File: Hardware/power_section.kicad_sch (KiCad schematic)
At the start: 38 parts, among them IC2 TPS54202HDDCR, U4 TLV743P, U6 TLV743P, U7 TLV743P

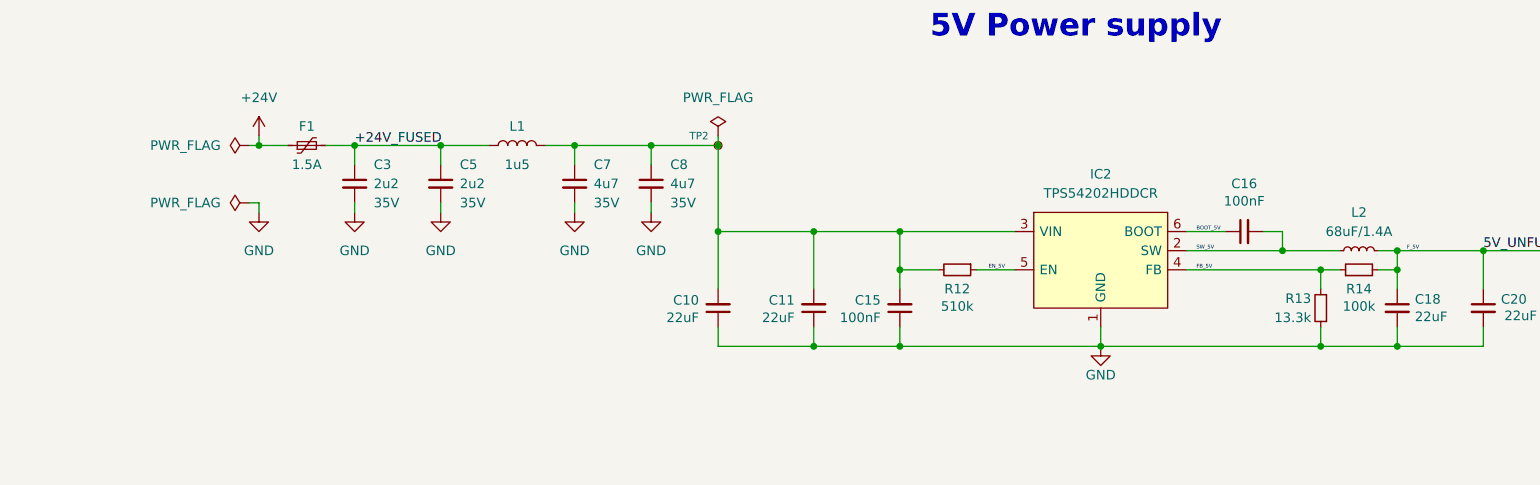
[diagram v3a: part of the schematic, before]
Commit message: Changes Vcc op-amps in brakes pressure (3V3 to 5V) and mcp6002 footprint (to MSOP8)
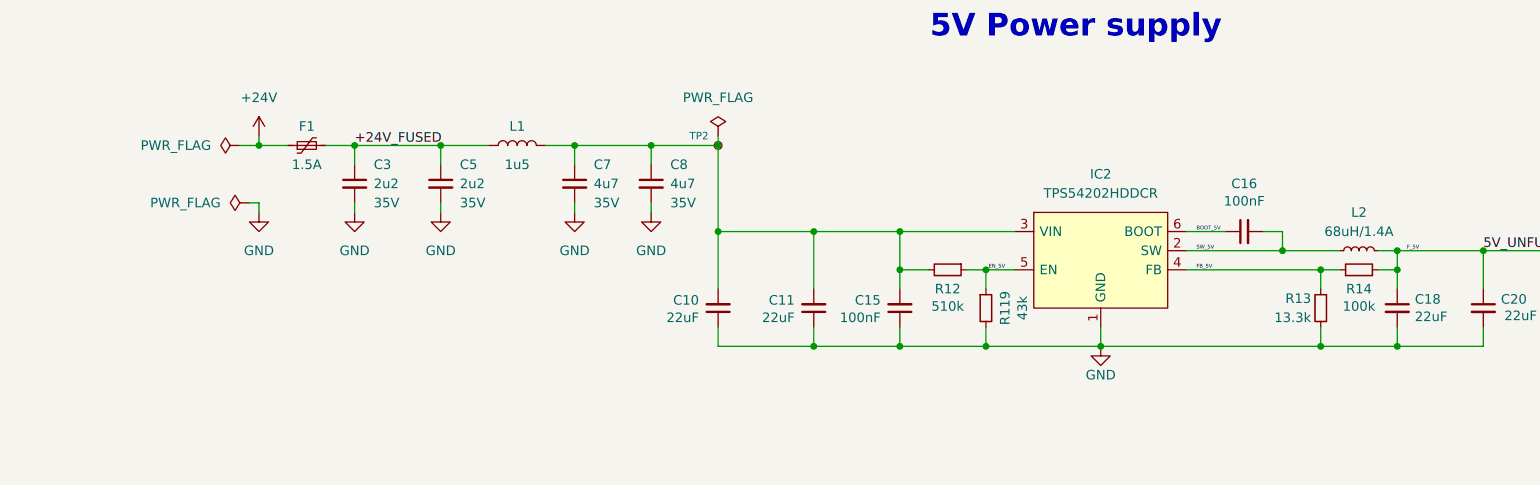
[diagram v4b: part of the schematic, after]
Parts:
- added R119: 43k, Resistor_SMD:R_0603_1608Metric, symbol Device:R_Small
- L2: value 68uF/1.4A -> 68uH/1.4A
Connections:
- net EN_5V: now also R119.1
- net GND: now also R119.2
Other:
- moved on the sheet: R12

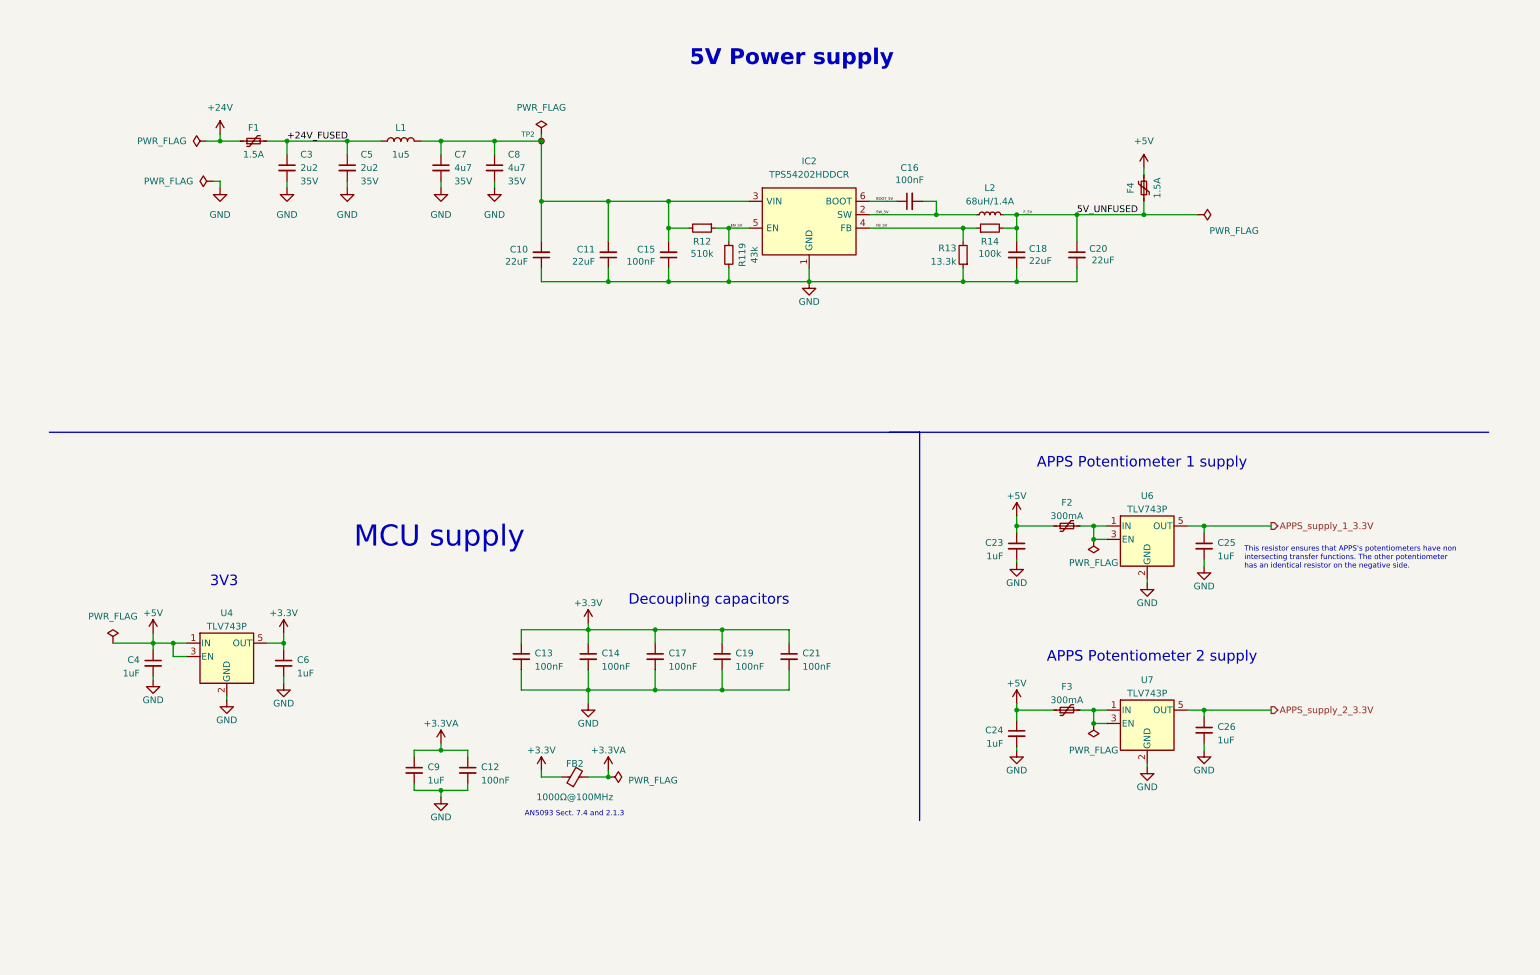
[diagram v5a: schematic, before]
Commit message: Created new hardware version 2.0
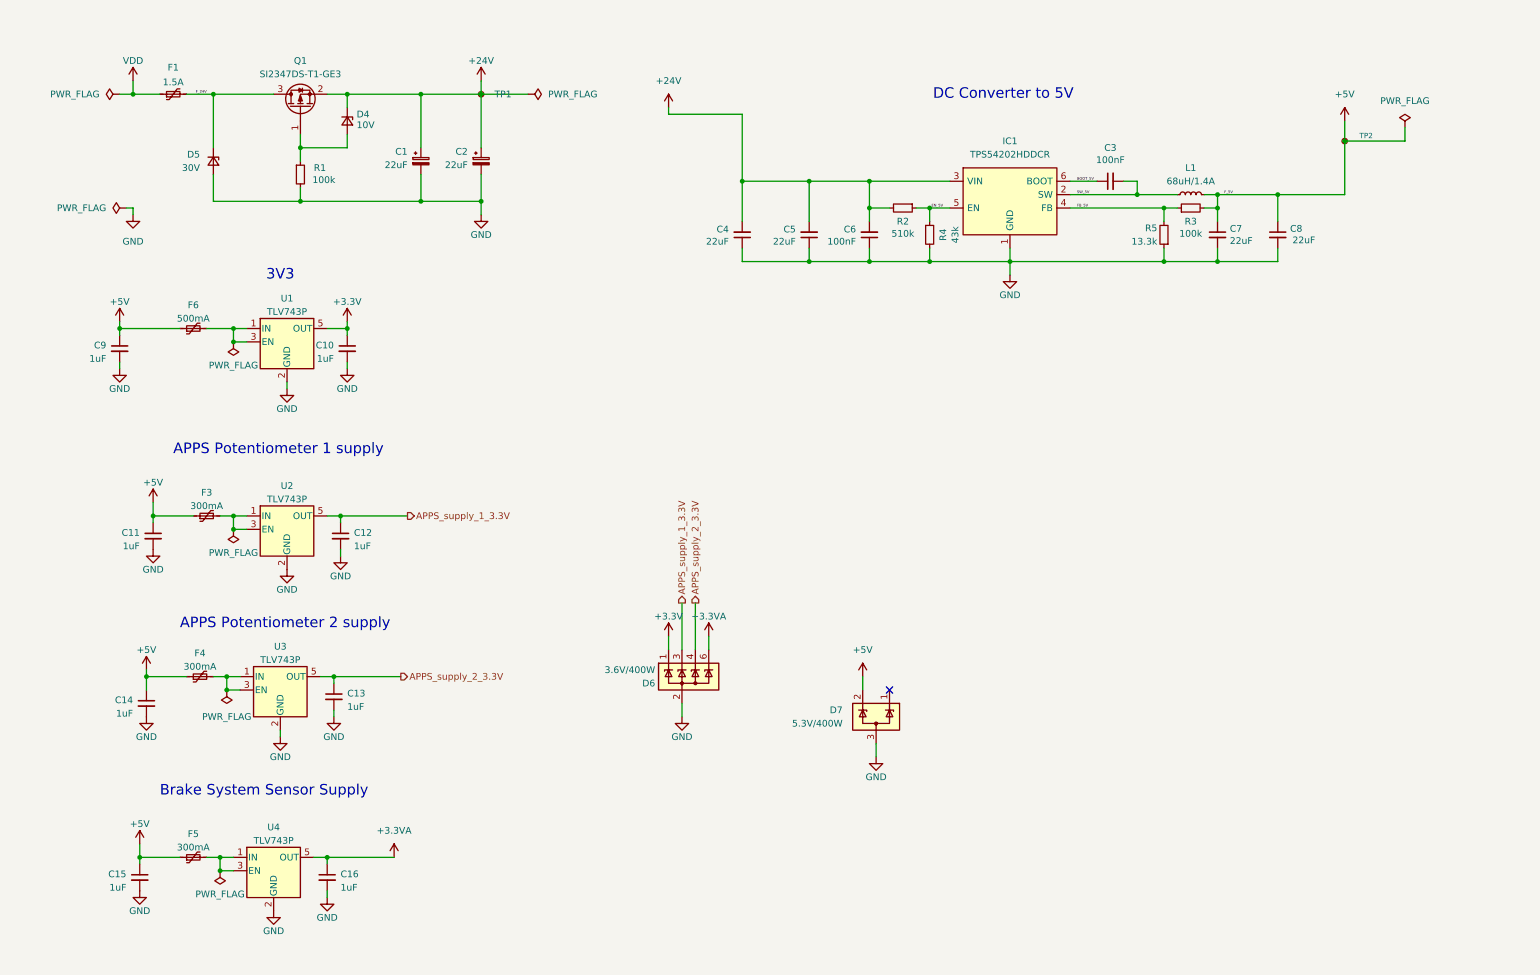
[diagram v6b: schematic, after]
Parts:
- removed C11, C18, C20: 22uF, Capacitor_SMD:C_0805_2012Metric, symbol Device:C_Small
- removed C12, C13, C14, C17, C19, C21: 100nF, Capacitor_SMD:C_0402_1005Metric_Pad0.74x0.62mm_HandSolder, symbol Device:C_Small
- removed F4: 1.5A, Fuse:Fuse_1812_4532Metric, symbol Device:Polyfuse_Small
- removed FB2: 1000Ω@100MHz, Inductor_SMD:L_0603_1608Metric, symbol Device:FerriteBead_Small
- removed L1: 1u5, Inductor_SMD:L_Abracon_ASPI-4030S, symbol Device:L
- removed R12: 510k, Resistor_SMD:R_0603_1608Metric, symbol Device:R_Small
- removed R13: 13.3k, Resistor_SMD:R_0603_1608Metric, symbol Device:R_Small
- removed R14: 100k, Resistor_SMD:R_0603_1608Metric, symbol Device:R_Small
- removed U6, U7: TLV743P, Package_TO_SOT_SMD:SOT-23-5_HandSoldering, symbol Regulator_Linear:TLV73330PDBV
- added C1, C2: 22uF, Capacitor_SMD:CP_Elec_4x5.8, symbol Device:C_Polarized_Small
- added D4: 10V, Diode_SMD:D_SOD-123, symbol Device:D_Zener_Small
- added D5: 30V, Diode_SMD:D_SOD-123, symbol Device:D_Zener_Small
- added D6: 3.6V/400W, Package_TO_SOT_SMD:SOT-23-6, symbol Power_Protection:ESDA5V3SC5
- added D7: 5.3V/400W, Package_TO_SOT_SMD:SOT-23-3, symbol Power_Protection:ESDA5V3L
- added F5: 300mA, Fuse:Fuse_0603_1608Metric_Pad1.05x0.95mm_HandSolder, symbol Device:Polyfuse_Small
- added F6: 500mA, Fuse:Fuse_0603_1608Metric_Pad1.05x0.95mm_HandSolder, symbol Device:Polyfuse_Small
- added Q1: SI2347DS-T1-GE3, Package_TO_SOT_SMD:SOT-23-3, symbol Transistor_FET:Q_PMOS_GSD
- added R1: 100k, Resistor_SMD:R_0603_1608Metric_Pad0.98x0.95mm_HandSolder, symbol Device:R_Small
- added R2: 510k, Resistor_SMD:R_0603_1608Metric, symbol Device:R_Small
- added R3: 100k, Resistor_SMD:R_0603_1608Metric, symbol Device:R_Small
- added R5: 13.3k, Resistor_SMD:R_0603_1608Metric, symbol Device:R_Small
- added TP1: TestPoint_Small, TestPoint:TestPoint_THTPad_D1.0mm_Drill0.5mm, symbol Connector:TestPoint_Small
- added U1, U2, U3: TLV743P, Package_TO_SOT_SMD:SOT-23-5_HandSoldering, symbol Regulator_Linear:TLV73330PDBV
- C10: value 22uF -> 1uF; footprint Capacitor_SMD:C_0805_2012Metric -> Capacitor_SMD:C_0603_1608Metric_Pad1.08x0.95mm_HandSolder; Manufacturer_Name MCASH21GCC7684MTCA1J -> (none); Manufacturer_Part_Number CL21A107MQYNNWE -> (none); Mouser Part Number 810-C2012X5R1V226MAC -> (none)
- C11: renamed from C23; footprint Capacitor_SMD:C_0402_1005Metric_Pad0.74x0.62mm_HandSolder -> Capacitor_SMD:C_0603_1608Metric_Pad1.08x0.95mm_HandSolder
- C12: renamed from C25; footprint Capacitor_SMD:C_0402_1005Metric_Pad0.74x0.62mm_HandSolder -> Capacitor_SMD:C_0603_1608Metric_Pad1.08x0.95mm_HandSolder
- C13: renamed from C26; footprint Capacitor_SMD:C_0402_1005Metric_Pad0.74x0.62mm_HandSolder -> Capacitor_SMD:C_0603_1608Metric_Pad1.08x0.95mm_HandSolder
- C14: renamed from C24; footprint Capacitor_SMD:C_0402_1005Metric_Pad0.74x0.62mm_HandSolder -> Capacitor_SMD:C_0603_1608Metric_Pad1.08x0.95mm_HandSolder
- C15, C16: value 100nF -> 1uF; footprint Capacitor_SMD:C_0603_1608Metric -> Capacitor_SMD:C_0603_1608Metric_Pad1.08x0.95mm_HandSolder; Manufacturer_Name -- -> (none); Manufacturer_Part_Number C0603C104J3RACTU -> (none); Mouser Part Number -- -> (none); Mouser Price/Stock https://www.mouser.pl/ProductDetail/KEMET/C0603C104J3RACTU?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 -> (none)
- C3: value 2u2 -> 100nF; footprint Capacitor_SMD:C_0805_2012Metric -> Capacitor_SMD:C_0603_1608Metric; Manufacturer_Name (none) -> --; Manufacturer_Part_Number (none) -> C0603C104J3RACTU; Mouser Part Number (none) -> --; Mouser Price/Stock (none) -> https://www.mouser.pl/ProductDetail/KEMET/C0603C104J3RACTU?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; Rated Voltage 35V -> (none)
- C4: value 1uF -> 22uF; footprint Capacitor_SMD:C_0402_1005Metric_Pad0.74x0.62mm_HandSolder -> Capacitor_SMD:C_0805_2012Metric; Manufacturer_Name (none) -> MCASH21GCC7684MTCA1J; Manufacturer_Part_Number (none) -> CL21A107MQYNNWE; Mouser Part Number (none) -> 810-C2012X5R1V226MAC
- C5: value 2u2 -> 22uF; Manufacturer_Name (none) -> MCASH21GCC7684MTCA1J; Manufacturer_Part_Number (none) -> CL21A107MQYNNWE; Mouser Part Number (none) -> 810-C2012X5R1V226MAC; Rated Voltage 35V -> (none)
- C6: value 1uF -> 100nF; footprint Capacitor_SMD:C_0402_1005Metric_Pad0.74x0.62mm_HandSolder -> Capacitor_SMD:C_0603_1608Metric; Manufacturer_Name (none) -> --; Manufacturer_Part_Number (none) -> C0603C104J3RACTU; Mouser Part Number (none) -> --; Mouser Price/Stock (none) -> https://www.mouser.pl/ProductDetail/KEMET/C0603C104J3RACTU?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
- C7, C8: value 4u7 -> 22uF; Manufacturer_Name (none) -> MCASH21GCC7684MTCA1J; Manufacturer_Part_Number (none) -> CL21A107MQYNNWE; Mouser Part Number (none) -> 810-C2012X5R1V226MAC; Rated Voltage 35V -> (none)
- C9: footprint Capacitor_SMD:C_0402_1005Metric_Pad0.74x0.62mm_HandSolder -> Capacitor_SMD:C_0603_1608Metric_Pad1.08x0.95mm_HandSolder
- renumbered F2 to F3, F3 to F4, IC2 to IC1, L2 to L1, R119 to R4
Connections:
- net 5V_UNFUSED is gone; now on net +5V: L1.2
- net +24V: now also C4.2, C5.2, C6.2, IC1.3 (VIN), C1.1, C2.1, D4.1 (K), Q1.2 (S), R2.2, TP1.1; no longer F1.1
- net +3.3V: now also C10.1, D6.1 (A), U1.5 (OUT); no longer C6.1, U4.5 (OUT)
- net +3.3VA: now also C16.1, U4.5 (OUT), D6.6 (A); no longer C9.1
- net +5V: now also C15.1, C7.1, C8.1, C9.1, TP2.1, D7.2 (K), F5.1, F6.1, R3.2; no longer C4.1, U4.1 (IN), U4.3 (EN)
- net APPS_supply_1_3.3V: now also D6.3 (A), U2.5 (OUT)
- net APPS_supply_2_3.3V: now also D6.4 (A), U3.5 (OUT)
- net BOOT_5V: now also C3.1; no longer C16.1
- net EN_5V: now also R2.1
- net FB_5V: now also R3.1, R5.2
- net GND: now also C10.2, C15.2, C16.2, C4.1, C5.1, C6.1, C1.2, C2.2, D5.2 (A), D6.2 (K), D6.5 (NC), D7.3 (A), R1.2, R5.1, U1.2 (GND), U2.2 (GND), U3.2 (GND); no longer C10.1, C15.1, C3.2, C4.2, C5.2, C6.2
- net SW_5V: now also C3.2; no longer C16.2
- net at F4.2: now also U3.1 (IN), U3.3 (EN)
- net at F3.2: now also U2.1 (IN), U2.3 (EN)
- removed net +24V_FUSED: C3.1, C5.1, F1.2
- new net: D4.2 (A), Q1.1 (G), R1.1
- new net: F5.2, U4.1 (IN), U4.3 (EN)
- new net: F6.2, U1.1 (IN), U1.3 (EN)
- new net F_24V: D5.1 (K), F1.2, Q1.3 (D)
- new net VDD: F1.1
- no-connect marks 0 -> 1
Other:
- note added: "Brake System Sensor Supply"
- note added: "DC Converter to 5V"
- note removed: "5V Power supply"
- note removed: "AN5093 Sect. 7.4 and 2.1.3"
- note removed: "Decoupling capacitors"
- note removed: "MCU supply"
- note removed: "This resistor ensures that APPS's potentiometers have non intersecting transfer functions. The other potentiometer has an identical resistor on the negative side."
- company: Author: Szymon Kostrubiec -> (none)
- title: Power section -> (none)
- moved on the sheet: C11, C12, C13, C14, F1, F3, F4, IC1, L1, R4
